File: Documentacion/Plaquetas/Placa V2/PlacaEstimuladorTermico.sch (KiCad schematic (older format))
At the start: 72 parts, among them J1 Conn_01x02, J10 Conn_01x04_Male, J2 DB9_Female_MountingHoles, J3 Conn_01x01, J4 Conn_01x01, J5 Conn_01x02, J6 Pulsador OFF, J7 Conn_02x05_Counter_Clockwise, J8 Conn_02x05_Counter_Clockwise, J9 Conn_01x04_Male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

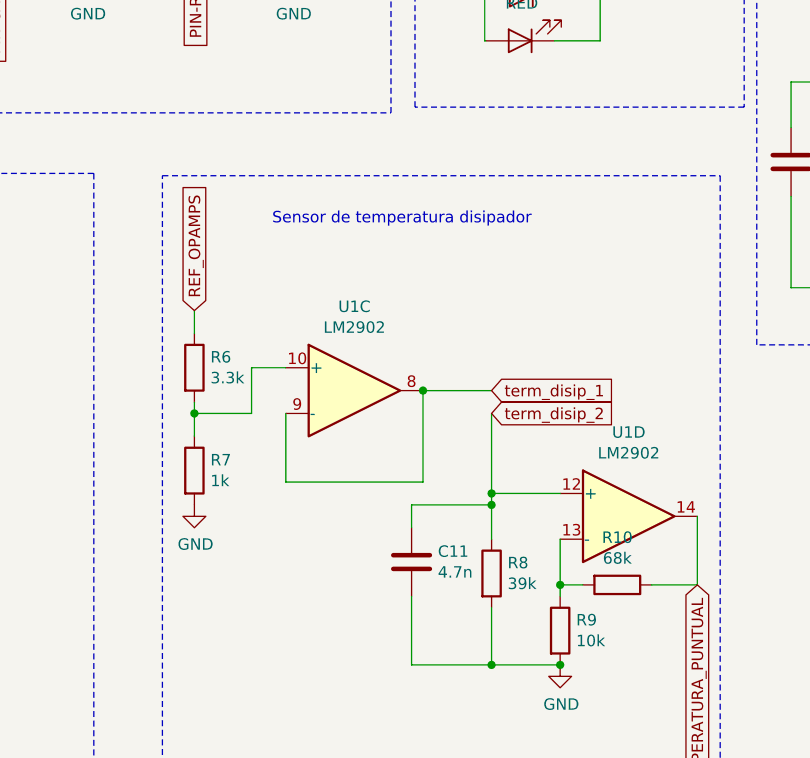
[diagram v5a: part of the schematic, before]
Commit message: simplification of the dissipator temperature measurement circuit and simplification of code
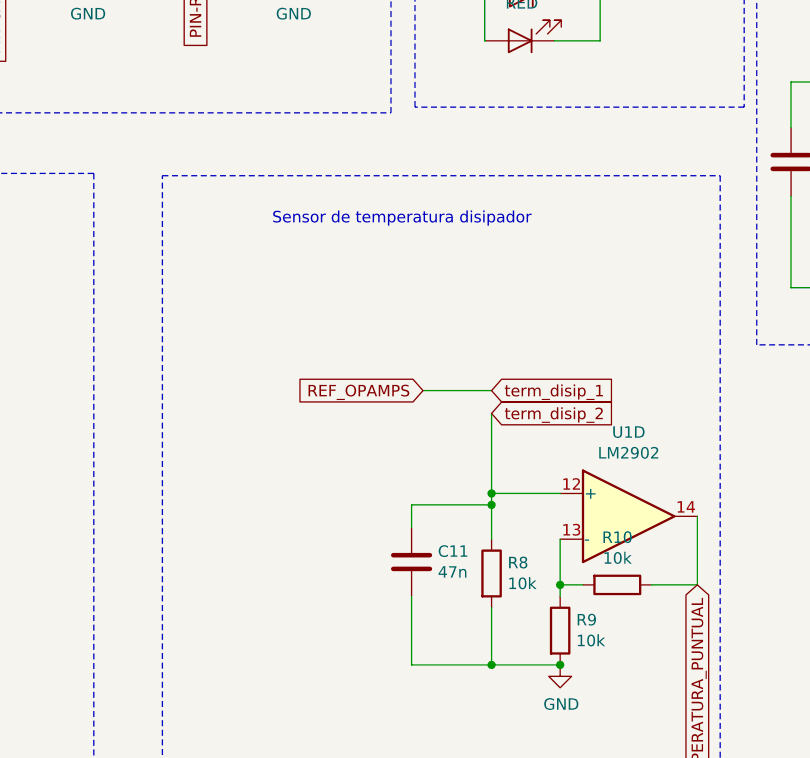
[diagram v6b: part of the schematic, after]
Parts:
- removed R6: 3.3k, Resistor_SMD:R_1206_3216Metric, symbol Device:R
- removed R7: 1k, Resistor_SMD:R_1206_3216Metric, symbol Device:R
- removed unit 3 of U1
- C11: value 4.7n -> 47n
- R10: value 68k -> 10k
- R8: value 39k -> 10k
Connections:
- wire segments 326 -> 317
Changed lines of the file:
@@
 EESchema Schematic File Version 4
-LIBS:PlacaEstimuladorTermico-cache
 EELAYER 30 0
 EELAYER END
@@
 $Comp
 L Amplifier_Operational:LM2902 U1
-U 3 1 5DB69274
-P 7990 8150
-F 0 "U1" H 7990 8517 50  0000 C CNN
-F 1 "LM2902" H 7990 8426 50  0000 C CNN
-F 2 "Package_DIP:DIP-14_W8.89mm_SMDSocket_LongPads" H 7940 8250 50  0001 C CNN
-F 3 "http://www.ti.com/lit/ds/symlink/lm2902-n.pdf" H 8040 8350 50  0001 C CNN
-	3    7990 8150
-	1    0    0    -1
-$EndComp
-$Comp
-L Amplifier_Operational:LM2902 U1
 U 4 1 5DB6A558
 P 9190 8700
@@
 Wire Wire Line
 	10300 6200 10650 6200
-Text GLabel 7290 7800 1    50   Input ~ 0
+Text GLabel 8290 8150 0    50   Input ~ 0
 REF_OPAMPS
-$Comp
-L Device:R R6
-U 1 1 5DCA69BD
-P 7290 8050
-F 0 "R6" H 7360 8096 50  0000 L CNN
-F 1 "3.3k" H 7360 8005 50  0000 L CNN
-F 2 "Resistor_SMD:R_1206_3216Metric" V 7220 8050 50  0001 C CNN
-F 3 "~" H 7290 8050 50  0001 C CNN
-	1    7290 8050
-	1    0    0    -1
-$EndComp
-$Comp
-L Device:R R7
-U 1 1 5DCA906F
-P 7290 8500
-F 0 "R7" H 7360 8546 50  0000 L CNN
-F 1 "1k" H 7360 8455 50  0000 L CNN
-F 2 "Resistor_SMD:R_1206_3216Metric" V 7220 8500 50  0001 C CNN
-F 3 "~" H 7290 8500 50  0001 C CNN
-	1    7290 8500
-	1    0    0    -1
-$EndComp
-Wire Wire Line
-	7290 7800 7290 7900
-Wire Wire Line
-	7290 8200 7290 8250
-Wire Wire Line
-	7690 8050 7540 8050
-Wire Wire Line
-	7540 8050 7540 8250
-Wire Wire Line
-	7540 8250 7290 8250
-Connection ~ 7290 8250
-Wire Wire Line
-	7290 8250 7290 8350
-Wire Wire Line
-	7690 8250 7690 8550
-Wire Wire Line
-	7690 8550 8290 8550
-Wire Wire Line
-	8290 8550 8290 8150
-$Comp
-L power:GND #PWR07
-U 1 1 5DCC00D9
-P 7290 8650
-F 0 "#PWR07" H 7290 8400 50  0001 C CNN
-F 1 "GND" H 7295 8477 50  0000 C CNN
-F 2 "" H 7290 8650 50  0001 C CNN
-F 3 "" H 7290 8650 50  0001 C CNN
-	1    7290 8650
-	1    0    0    -1
-$EndComp
 Wire Wire Line
 	8290 8150 8590 8150
-Connection ~ 8290 8150
 Wire Wire Line
 	8590 8250 8590 8600
@@
 P 8590 8950
 F 0 "R8" H 8660 8996 50  0000 L CNN
-F 1 "39k" H 8660 8905 50  0000 L CNN
+F 1 "10k" H 8660 8905 50  0000 L CNN
 F 2 "Resistor_SMD:R_1206_3216Metric" V 8520 8950 50  0001 C CNN
 F 3 "~" H 8590 8950 50  0001 C CNN
@@
 P 9140 9000
 F 0 "R10" V 8933 9000 50  0000 C CNN
-F 1 "68k" V 9024 9000 50  0000 C CNN
+F 1 "10k" V 9024 9000 50  0000 C CNN
 F 2 "Resistor_SMD:R_1206_3216Metric" V 9070 9000 50  0001 C CNN
 F 3 "~" H 9140 9000 50  0001 C CNN
@@
 P 8240 8900
 F 0 "C11" H 8355 8946 50  0000 L CNN
-F 1 "4.7n" H 8355 8855 50  0000 L CNN
+F 1 "47n" H 8355 8855 50  0000 L CNN
 F 2 "Capacitor_SMD:C_1206_3216Metric_Pad1.42x1.75mm_HandSolder" H 8278 8750 50  0001 C CNN
 F 3 "~" H 8240 8900 50  0001 C CNN
